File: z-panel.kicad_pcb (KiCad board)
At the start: 2 copper layers, 80 x 80 mm, 43 parts, among them J1 MOLEX_FFC-14, J2 PC104PTH, J3 PC104PTH, J4 PC104PTH, J5 PC104PTH, J6 TEST_1P, J7 TEST_1P, J8 TEST_1P, U100 OPA380, U110 OPA380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

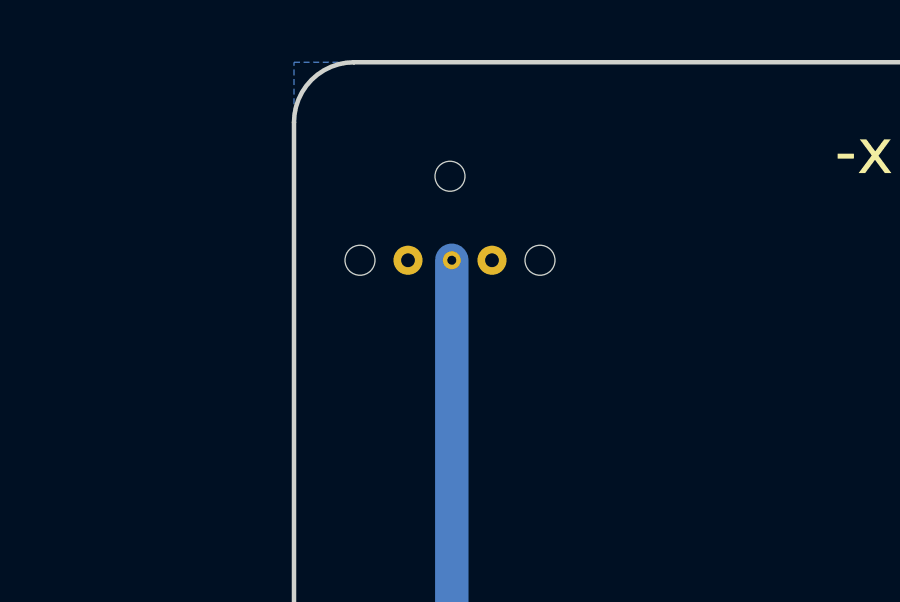
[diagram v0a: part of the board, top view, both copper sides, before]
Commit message: fixed GPS coax entry. Closes #1
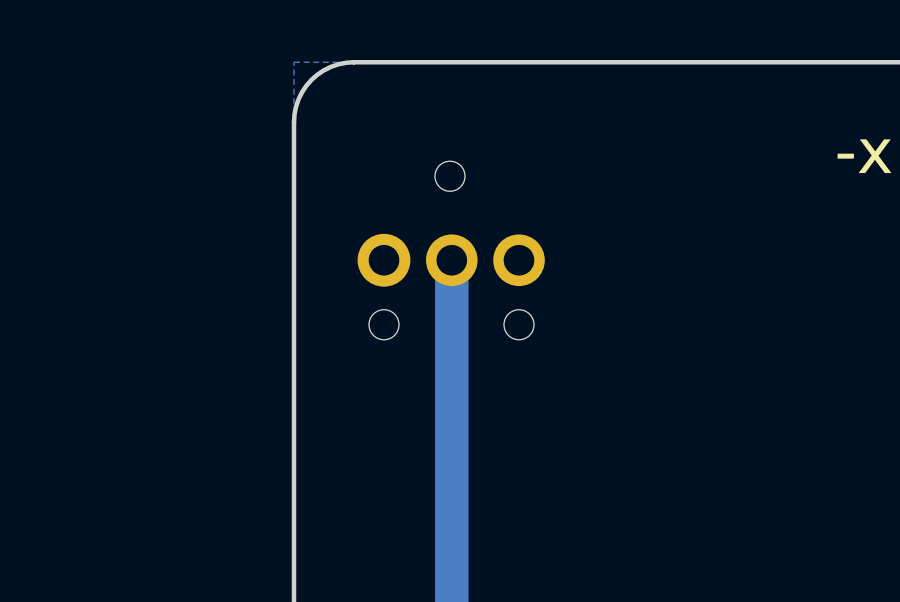
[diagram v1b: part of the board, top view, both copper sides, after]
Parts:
- moved REF** 2.29 mm to (146.0, 68.8)
- moved REF** 2.26 mm to (150.5, 68.8)
- moved J7 0.90 mm to (150.5, 66.6)
- moved J8 0.80 mm to (146.0, 66.6)
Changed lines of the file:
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@@
     (links 74)
     (no_connects 0)
-    (area 85.366646 41.900001 201.571429 150.35)
+    (area 85.366646 41.900001 190.275 148.850001)
     (thickness 0.8)
     (drawings 54)
@@
     (mod_text_size 1 1)
     (mod_text_width 0.15)
-    (pad_size 0.6 0.6)
-    (pad_drill 0.3)
+    (pad_size 1.76 1.76)
+    (pad_drill 1.02)
     (pad_to_mask_clearance 0.03)
     (aux_axis_origin 0 0)
@@
   )
   (module SFUSat:NPTH-1mm (layer F.Cu)
-    (at 151.2 66.6)
+    (at 150.5 68.75)
     (fp_text reference REF** (at 0 2) (layer F.SilkS) hide
       (effects (font (size 1 1) (thickness 0.15)))
@@
       (effects (font (size 1 1) (thickness 0.15)) (justify mirror))
     )
-    (pad 1 thru_hole circle (at -3.74 0.6) (size 0.6 0.6) (drill 0.3) (layers *.Cu)
+    (pad 1 thru_hole circle (at -3.74 0.6) (size 1.72 1.72) (drill 1.02) (layers *.Cu *.Mask)
       (net 1 "Net-(A1-Pad1)") (zone_connect 2))
   )
   (module SFUSat:NPTH-1mm (layer F.Cu)
-    (at 145.2 66.6)
+    (at 146 68.75)
     (fp_text reference REF** (at 0 2) (layer F.SilkS) hide
       (effects (font (size 1 1) (thickness 0.15)))
@@
   )
   (module SFUSat:via-0.97mm (layer F.Cu)
-    (at 149.6 66.6)
+    (at 150.5 66.6)
     (fp_text reference J7 (at 0.0635 2.032) (layer F.SilkS) hide
       (effects (font (size 1 1) (thickness 0.15)))
@@
       (effects (font (size 1 1) (thickness 0.15)))
     )
-    (pad 1 thru_hole circle (at 0 0) (size 0.97 0.97) (drill 0.46) (layers *.Cu)
+    (pad 1 thru_hole circle (at 0 0) (size 1.72 1.72) (drill 1.02) (layers *.Cu *.Mask)
       (net 10 GND) (zone_connect 2))
   )
   (module SFUSat:via-0.97mm (layer F.Cu)
-    (at 146.8 66.6)
+    (at 146 66.6)
     (fp_text reference J8 (at 0.0635 2.032) (layer F.SilkS) hide
       (effects (font (size 1 1) (thickness 0.15)))
@@
       (effects (font (size 1 1) (thickness 0.15)))
     )
-    (pad 1 thru_hole circle (at 0 0) (size 0.97 0.97) (drill 0.46) (layers *.Cu)
+    (pad 1 thru_hole circle (at 0 0) (size 1.76 1.76) (drill 1.02) (layers *.Cu *.Mask)
       (net 10 GND) (zone_connect 2))
   )

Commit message: solder mask fixed to conform to min 150um webbing requirement
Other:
- rule pad_to_mask_clearance: 0.03 -> 0.02
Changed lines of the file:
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@@
     (pad_size 1.76 1.76)
     (pad_drill 1.02)
-    (pad_to_mask_clearance 0.03)
+    (pad_to_mask_clearance 0.02)
     (aux_axis_origin 0 0)
     (visible_elements FFFFFF7F)
